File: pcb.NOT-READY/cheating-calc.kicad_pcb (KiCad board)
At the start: 2 copper layers, 72 x 22 mm, 22 parts, among them J1 Conn_01x04, J2 Conn_01x04, Q1 MMBF170, Q2 MMBF170, U1 ESP32-C3-MINI-1-N4, U2 AP7215-33YG-13

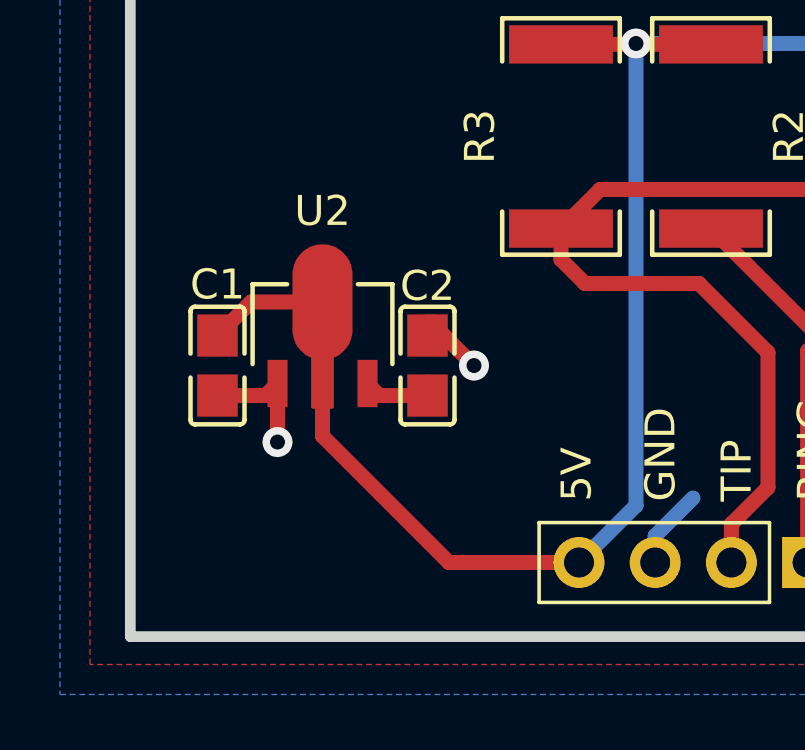
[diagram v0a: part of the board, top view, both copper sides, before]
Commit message: update to use a cheaper more avalible LDO
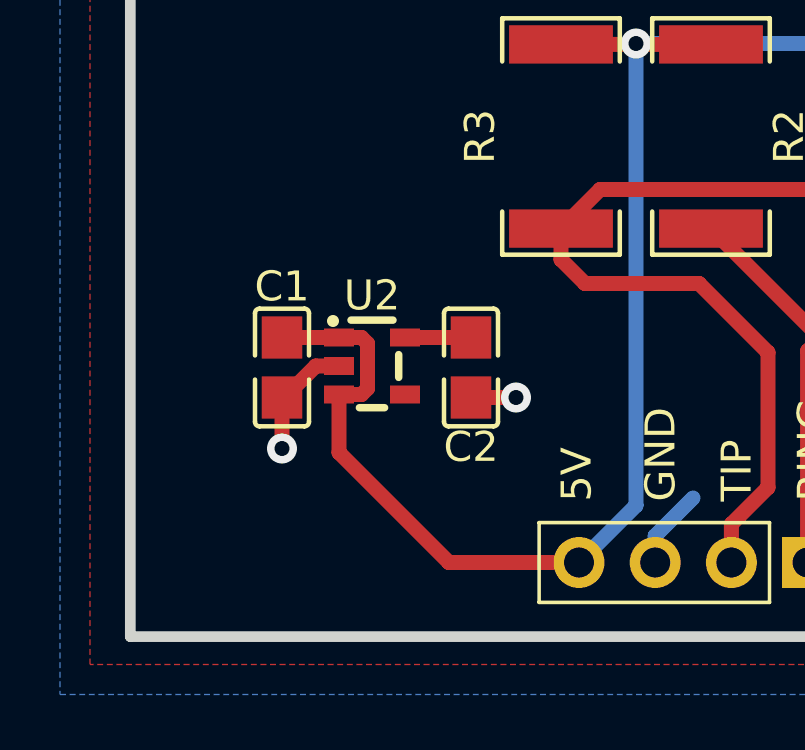
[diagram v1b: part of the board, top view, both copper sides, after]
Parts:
- U2: value AP7215-33YG-13 -> TPLP5907MFX-3.3; footprint easyeda2kicad:SOT-89-3_L4.5-W2.5-P1.50-LS4.2-BR -> easyeda2kicad:SOT-23-5_L2.9-W1.6-P0.95-LS2.8-BR
- moved C1 2.15 mm to (90.4, 65.1)
- moved U2 1.82 mm to (93.4, 65.0), turned to 180 degrees
- moved C2 1.45 mm to (96.7, 65.1), turned to -90 degrees
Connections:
- U2 pad 1: GND -> +5V
- U2 pad 2: +5V -> GND
- U2 pad 3: +3.3V -> +5V
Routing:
- net +5V: track 88.8 -> 87.0 mm
- net GND: track 106.5 -> 105.2 mm
